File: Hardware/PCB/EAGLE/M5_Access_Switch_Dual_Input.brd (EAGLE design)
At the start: 20.2 x 36 mm, 13 parts

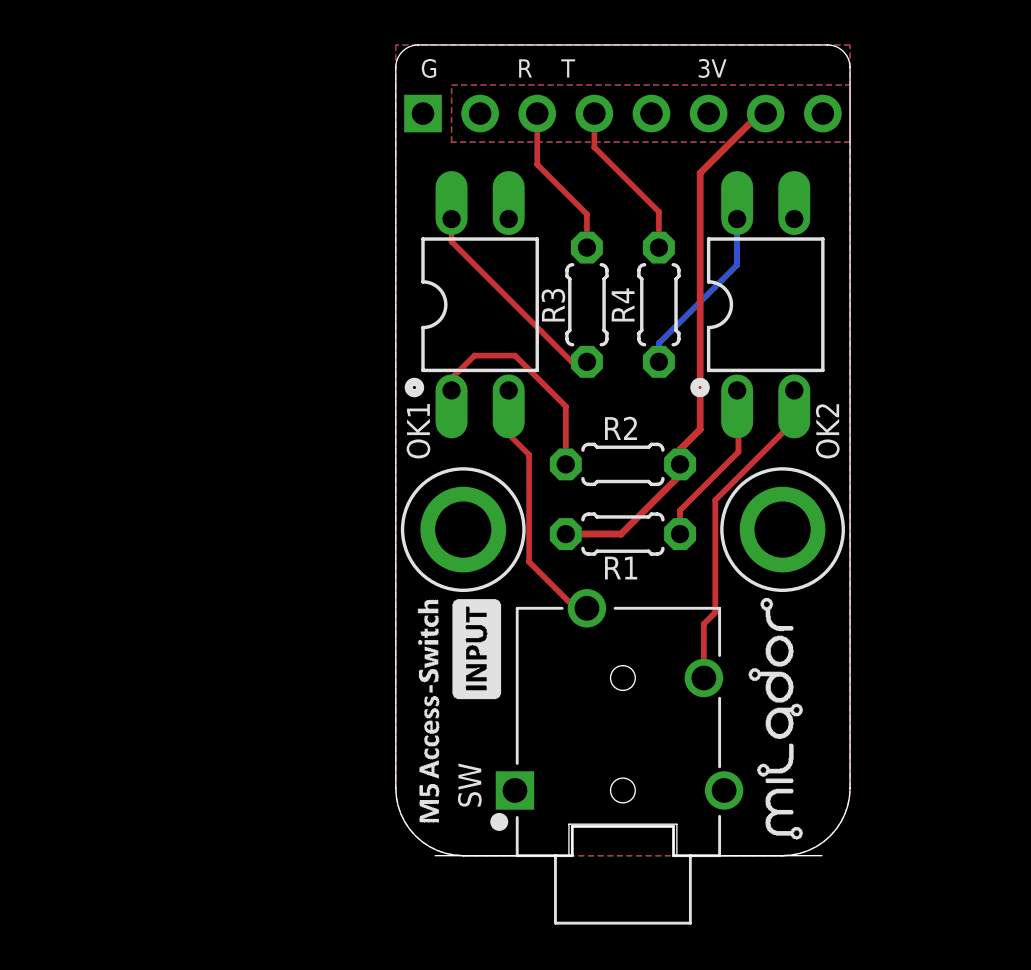
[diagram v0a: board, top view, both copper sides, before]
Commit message: Changed the design to dual mono jacks
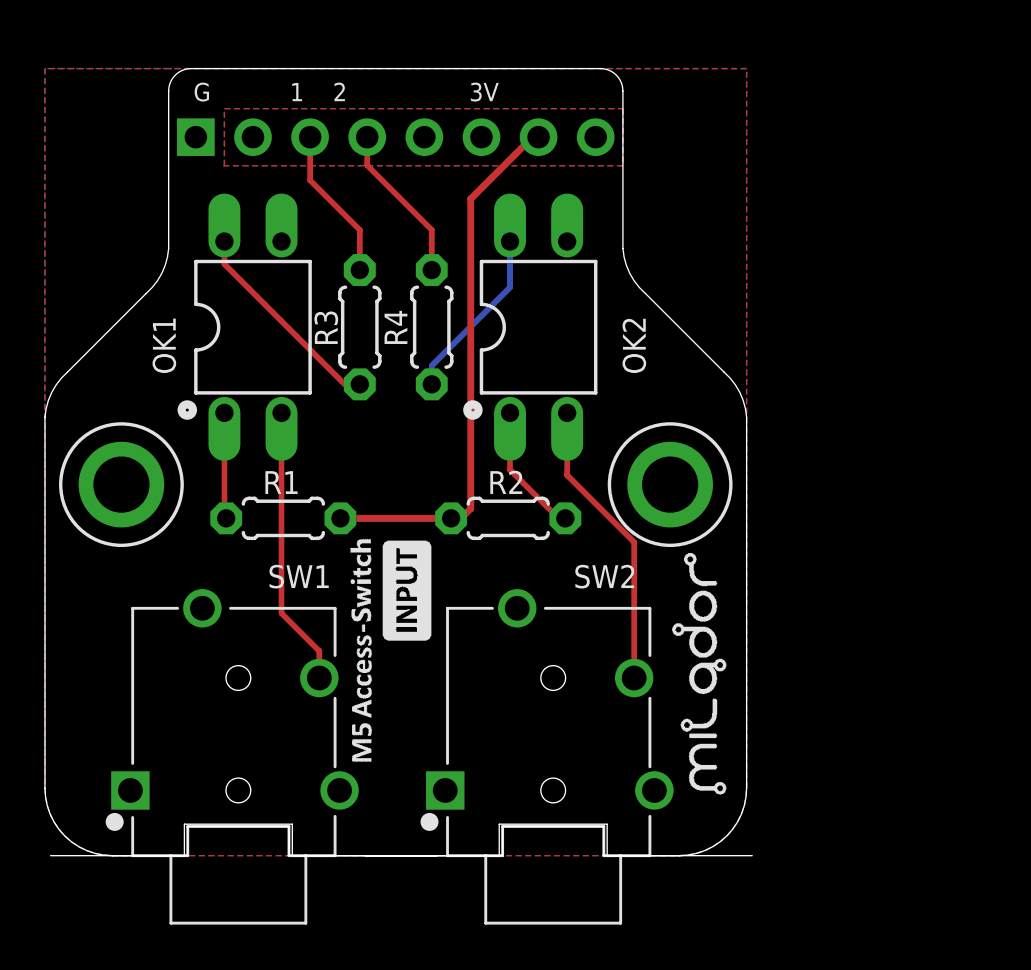
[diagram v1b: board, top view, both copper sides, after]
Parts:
- removed SW: SJ-43514, milador:CUI_SJ-43514
- added SW1, SW2: SJ-43514, milador:CUI_SJ-43514
- moved H1 15.3 mm to (-12.2, 16.5)
- moved R1 15.1 mm to (-5.00, 15.0), turned to 180 degrees
- moved JP1 10.2 mm to (0.00, 31.9)
- moved OK1 10.1 mm to (-6.35, 23.5)
- moved OK2 10.1 mm to (6.35, 23.5)
- moved R3 10.1 mm to (-1.60, 23.5)
- moved R4 10.1 mm to (1.60, 23.5)
- moved R2 5.64 mm to (5.00, 15.0), turned to 0 degrees
- moved H2 5.39 mm to (12.2, 16.5)
- moved LABEL_INPUT_TOP 4.05 mm to (0.50, 11.8)
- moved LABEL_DEVICE_TOP 4.04 mm to (-1.40, 9.10)
- moved LABEL_LOGO_TOP 3.94 mm to (14.0, 7.40)
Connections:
- net GND: now also SW1.1, SW1.3, SW1.4, SW2.1, SW2.3, SW2.4; no longer SW.1, SW.4
- net N$1: now also R1.2; no longer R2.2
- net N$14: now also R2.2; no longer R1.2
- net N$23: now also SW2.2; no longer SW.2
- net N$3: now also SW1.2; no longer SW.3
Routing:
- net N$1: track 9.54 -> 4.72 mm
- net N$14: track 7.49 -> 5.88 mm
- net N$23: track 14.5 -> 13.0 mm
- net N$3: track 11.4 -> 12.5 mm
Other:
- board size 20.2 x 36 mm -> 31.2 x 35 mm
- board text added: "G 1 2 3V"
- board text removed: "G R T 3V"
- board text removed: "R"
